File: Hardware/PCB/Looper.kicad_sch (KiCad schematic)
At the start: 63 parts, among them J1 Out right, J10 Audio from Daisy, connect to 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, J13 Audio to Daisy, connect to J13, J14 Audio from Daisy, connect to 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, J15 Audio input, connect to J18, J16 Audio output, connect to J17, J17 Audio output, connect to J16, J18 Audio input, connect to J15, J2 In left, J3 Trig Loop, J4 Out left, J5 In right, J6 Eurorack_Power, J9 Audio to Daisy, connect to J13, U1 TL074, U2 TL074

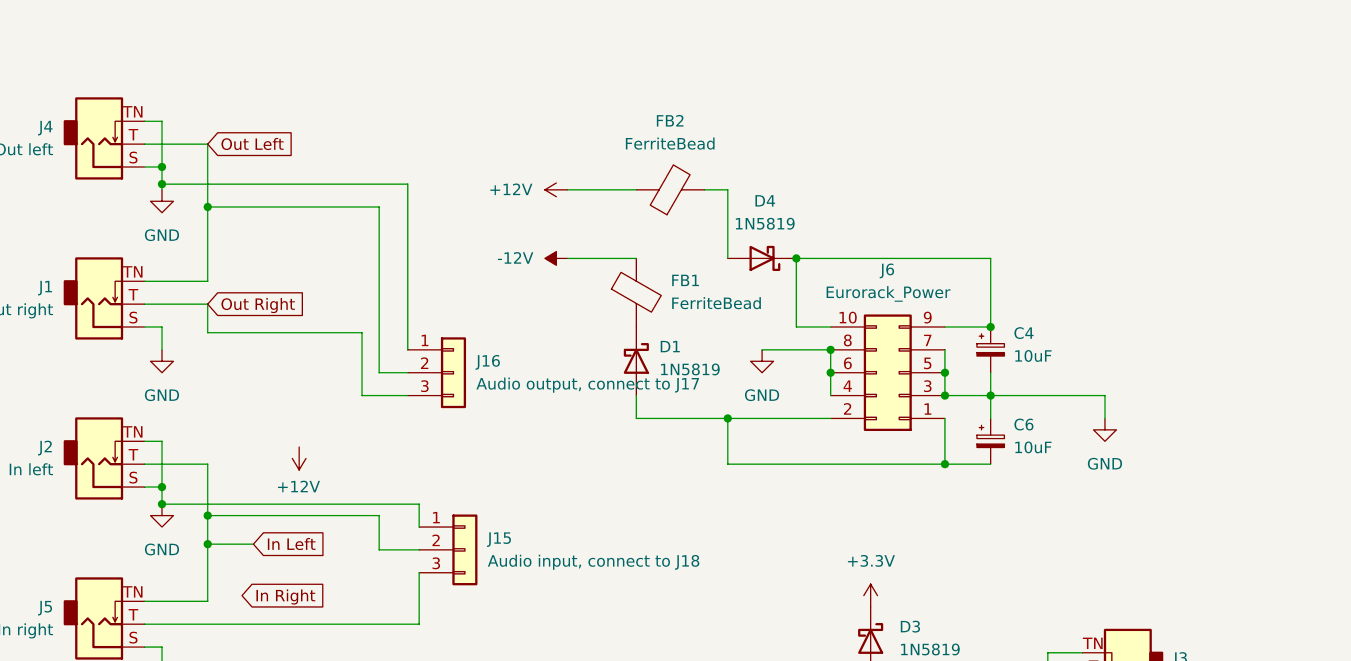
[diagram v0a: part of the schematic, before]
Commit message: Fixed power diode polarity
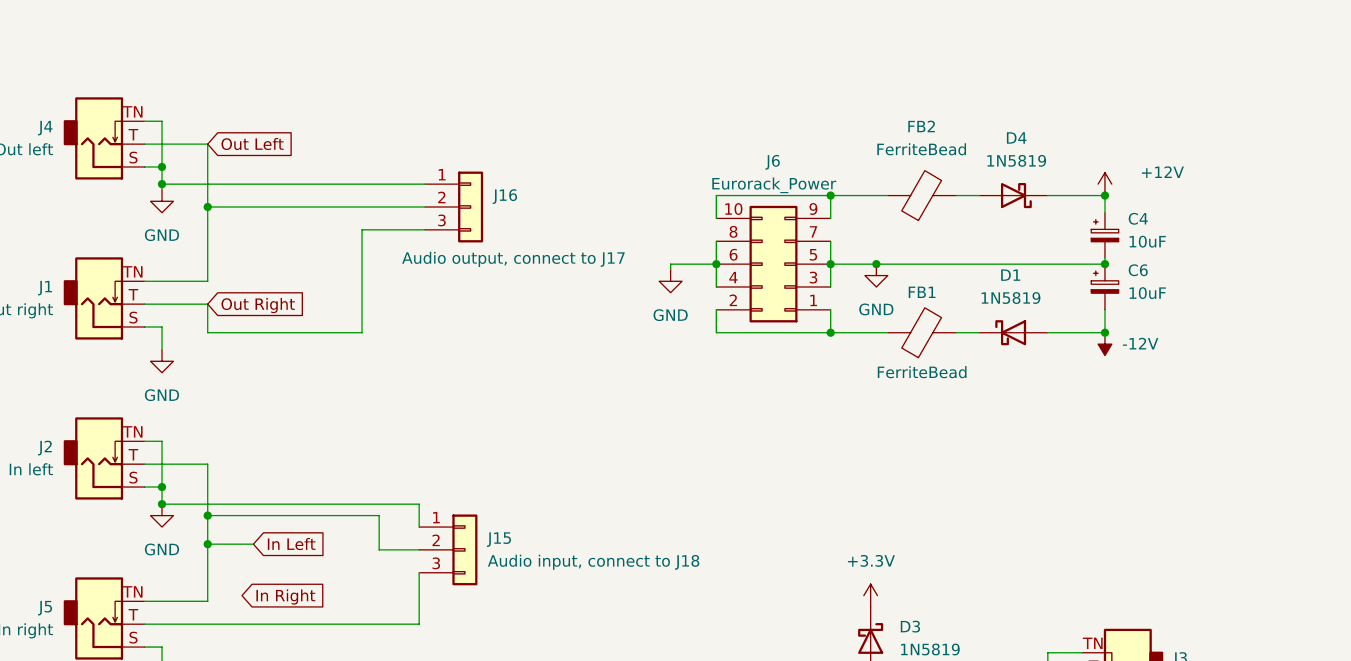
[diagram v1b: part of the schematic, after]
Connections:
- net +12V: now also C4.1, D4.1 (K); no longer FB2.1
- net -12V: now also C6.2, D1.2 (A); no longer FB1.1
- net at J6.10 (Pin_10), J6.9 (Pin_9): now also FB2.1; no longer C4.1, D4.1 (K)
- net at J6.1 (Pin_1), J6.2 (Pin_2): now also FB1.1; no longer C6.2, D1.2 (A)
- net at S1.1: now also A1.15 (USART1_RX)
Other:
- moved on the sheet: C4, C6, D1, D4, FB1, FB2, J16, J6

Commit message: new intracard connections
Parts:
- removed J10: Audio from Daisy, connect to J14, Connector_PinHeader_2.54mm:PinHeader_1x03_P2.54mm_Vertical, symbol Connector_Generic:Conn_01x03
- removed J13, J9: Audio to Daisy, connect to J13, Connector_PinHeader_2.54mm:PinHeader_1x03_P2.54mm_Vertical, symbol Connector_Generic:Conn_01x03
- removed J14: Audio from Daisy, connect to J10, Connector_PinHeader_2.54mm:PinHeader_1x03_P2.54mm_Vertical, symbol Connector_Generic:Conn_01x03
- removed J15: Audio input, connect to J18, Connector_PinHeader_2.54mm:PinHeader_1x03_P2.54mm_Vertical, symbol Connector_Generic:Conn_01x03
- removed J16: Audio output, connect to J17, Connector_PinHeader_2.54mm:PinHeader_1x03_P2.54mm_Vertical, symbol Connector_Generic:Conn_01x03
- removed J17: Audio output, connect to J16, Connector_PinHeader_2.54mm:PinHeader_1x03_P2.54mm_Vertical, symbol Connector_Generic:Conn_01x03
- removed J18: Audio input, connect to J15, Connector_PinHeader_2.54mm:PinHeader_1x03_P2.54mm_Vertical, symbol Connector_Generic:Conn_01x03
- added J11, J12, J7, J8: Conn_01x05, Connector_PinHeader_2.54mm:PinHeader_1x05_P2.54mm_Vertical, symbol Connector_Generic:Conn_01x05
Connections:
- net Out_R is gone; now on net DAISY_AUDIO_OUT_R: A1.19 (AUDIO_OUT_R)
- net +12V: now also J11.5 (Pin_5), J7.5 (Pin_5)
- net GND: now also J12.1 (Pin_1), J8.1 (Pin_1)
- net In Left: now also R16.1, J11.1 (Pin_1), J7.1 (Pin_1)
- net In Right: now also J5.T, R22.1, J12.2 (Pin_2), J8.2 (Pin_2)
- net Out Left: now also R5.1, U1.3 (+), J11.4 (Pin_4), J7.4 (Pin_4)
- net Out Right: now also R9.1, U1.10 (+), J12.4 (Pin_4), J8.4 (Pin_4)
- net at S1.1: now also A1.15 (USART1_RX)
- net DAISY_AUDIO_OUT_R: now reaches R21.2
- net DAISY_AUDIO_OUT_R: now also J12.3 (Pin_3), J8.3 (Pin_3)
- net DAISY_AUDIO_IN_L: now reaches A1.16 (AUDIO_IN_L)
- net DAISY_AUDIO_IN_L: now also R8.2, J11.3 (Pin_3), J7.3 (Pin_3)
- net DAISY_AUDIO_IN_R: now reaches A1.17 (AUDIO_IN_R)
- net DAISY_AUDIO_IN_R: now also R12.2, J12.5 (Pin_5), J8.5 (Pin_5)
- net DAISY_AUDIO_OUT_L: now reaches A1.18 (AUDIO_OUT_L)
- net DAISY_AUDIO_OUT_L: now also R14.2, J11.2 (Pin_2), J7.2 (Pin_2)
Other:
- moved on the sheet: J1, J2, J4, J5

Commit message: more labels
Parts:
- added J9: Conn_01x20_MountingPin, Connector_PinHeader_2.54mm:PinHeader_1x20_P2.54mm_Vertical, symbol Connector_Generic_MountingPin:Conn_01x20_MountingPin
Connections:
- net DAISY_AUDIO_IN_L: now also J9.16 (Pin_16)
- net DAISY_AUDIO_IN_R: now also J9.17 (Pin_17)
- net DAISY_AUDIO_OUT_L: now also J9.18 (Pin_18)
- net DAISY_AUDIO_OUT_R: now also J9.19 (Pin_19)
- net GND: now also J9.20 (Pin_20)
- net at R4.1: now also SW4.4; no longer A1.3 (SDMMC1_D2)
- net at R4.2: now also A1.3 (SDMMC1_D2), J9.3 (Pin_3); no longer SW4.4
- net at S1.1: now also A1.15 (USART1_RX), J9.15 (Pin_15)
- net at A1.2 (SDMMC1_D3), SW4.1: now also J9.2 (Pin_2)
- net at A1.4 (SDMMC1_D1), SW4.3: now also J9.4 (Pin_4)
- net at A1.14 (USART1_TX), S2.1: now also J9.14 (Pin_14)
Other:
- moved on the sheet: C1, C11, C12, C4, C5, C6, D1, D4, FB1, FB2, J1, J6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

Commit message: Endret hele leveller
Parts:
- removed D2, D3: 1N5819, Diode_SMD:D_SOD-123, symbol Device:D_Schottky
- added C13: 560pF, Capacitor_SMD:C_0603_1608Metric, symbol Device:C_Small
- added C14: 47pF, Capacitor_SMD:C_0603_1608Metric, symbol Device:C_Small
- added Q1: MMBT3904, Package_TO_SOT_SMD:SOT-23, symbol Transistor_BJT:MMBT3904
- added R23, R24, R25: 100K, Resistor_SMD:R_0603_1608Metric, symbol Device:R
- added R26: 10K, Resistor_SMD:R_0603_1608Metric, symbol Device:R
- added R27: 1K, Resistor_SMD:R_0603_1608Metric, symbol Device:R
- added R28: 1M, Resistor_SMD:R_0603_1608Metric, symbol Device:R
- C2: value 560pF -> 47pF; LCSC C458906 -> C1671
- R11: value 10K -> 100K; LCSC C25804 -> C25803
- R5: value 2M -> 10K; LCSC C22976 -> C25804
- R9: value 2M -> 100K; LCSC C22976 -> C25803
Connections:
- net +12V: now also J11.1 (Pin_1), J7.1 (Pin_1); no longer J11.5 (Pin_5), J7.5 (Pin_5)
- net +3.3V: now also R26.1
- net DAISY_AUDIO_IN_L: now also J12.2 (Pin_2), J8.2 (Pin_2), R16.1; no longer J11.3 (Pin_3), J7.3 (Pin_3), R8.2
- net DAISY_AUDIO_IN_R: now also J12.3 (Pin_3), J8.3 (Pin_3), R22.1; no longer J12.5 (Pin_5), J8.5 (Pin_5), R12.2
- net DAISY_AUDIO_OUT_L: now also J12.4 (Pin_4), J8.4 (Pin_4), R7.1; no longer J11.2 (Pin_2), J7.2 (Pin_2), R14.2
- net DAISY_AUDIO_OUT_R: now also J12.5 (Pin_5), J8.5 (Pin_5), R5.2; no longer J12.3 (Pin_3), J8.3 (Pin_3), R21.2
- net GND: now also J1.TN, J5.TN, U1.10 (+), U1.3 (+), Q1.2 (E), R28.2; no longer R5.2, R9.2
- net In Left: now also J11.2 (Pin_2), J7.2 (Pin_2), R17.2; no longer J11.1 (Pin_1), J5.TN, J7.1 (Pin_1), R16.1
- net In Right: now also J11.3 (Pin_3), J7.3 (Pin_3), R18.2; no longer J12.2 (Pin_2), J8.2 (Pin_2), R22.1
- net Out Left: now also R8.1; no longer J1.TN, R5.1, U1.3 (+)
- net Out Right: now also J11.5 (Pin_5), J7.5 (Pin_5), R12.2; no longer J12.4 (Pin_4), J8.4 (Pin_4), R9.1, U1.10 (+)
- net at SW4.4: now also R4.2; no longer R4.1
- net SWITCH_4_RED: now reaches A1.3 (SDMMC1_D2), J9.3 (Pin_3)
- net SWITCH_4_RED: now also R4.1; no longer R4.2
- net at J3.T: now also R11.2; no longer A1.22 (ADC_INP10)
- net at C10.2, R19.2: now also R18.1, U2.2 (-); no longer R21.1, U2.13 (-)
- net at C10.1, R19.1, R20.2: now also U2.1; no longer U2.14
- net CLEAR_GPIO: now reaches S1.1
- net CLEAR_GPIO: now also A1.15 (USART1_RX), J9.15 (Pin_15)
- net SWITCH_4_GPIO: now reaches A1.2 (SDMMC1_D3), J9.2 (Pin_2), SW4.1
- net SWITCH_4_GREEN: now reaches A1.4 (SDMMC1_D1), J9.4 (Pin_4), SW4.3
- net at R6.2, U1.6 (-): now also C14.1, R24.1; no longer C2.1, R7.1
- net RECORD_GPIO: now reaches A1.23 (ADC_INP15)
- net RECORD_GPIO: now also S2.1
- net SWITCH_1_GREEN: now reaches A1.27 (ADC_INP11), SW1.3
- net SWITCH_1_RED: now reaches A1.28 (ADC1_INP4), R3.2
- net SWITCH_1_GPIO: now reaches A1.29 (DAC1_OUT2), SW1.1
- net SWITCH_2_RED: now reaches A1.30 (DAC1_OUT1), SW2.4
- net SWITCH_2_GPIO: now reaches A1.31 (SAI2_MCLK_B), SW2.2
- net at R2.2: now also SW2.3; no longer A1.32 (SAI2_SD_B)
- net SWITCH_3_GREEN: now reaches A1.33 (SAI2_SD_A), SW3.3
- net SWITCH_3_GPIO: now reaches A1.34 (SAI2_FS_B), SW3.1
- net at R1.1: now also SW3.4; no longer A1.35 (SAI2_SCK_B)
- net at C7.1, R13.1: now also R17.1, U2.6 (-); no longer R14.1, U2.2 (-)
- net SWITCH_2_GREEN: now reaches R2.1
- net SWITCH_2_GREEN: now also A1.32 (SAI2_SD_B); no longer SW2.3
- net at C7.2, R13.2, R15.2: now also U2.7; no longer U2.1
- net SWITCH_3_RED: now reaches R1.2
- net SWITCH_3_RED: now also A1.35 (SAI2_SCK_B); no longer SW3.4
- new net: C14.2, R24.2, R8.2, U1.7
- new net: C3.1, R20.1, R21.2, U2.13 (-)
- new net: C3.2, R21.1, R22.2, U2.14
- new net: C9.1, R10.1, R9.2, U1.14
- new net: C9.2, R5.1, R9.1, U1.13 (-)
- new net: C13.2, R14.1, R16.2, U2.8
- new net: C13.1, R14.2, R15.1, U2.9 (-)
- new net: C8.1, R23.1, R7.2, U1.9 (-)
- new net: C2.1, R12.1, R25.2, U1.1
- new net: C2.2, R10.2, R25.1, U1.2 (-)
- new net: C8.2, R23.2, R6.1, U1.8
- new net: Q1.3 (C), R26.2, R27.2
- new net: Q1.1 (B), R11.1, R28.1
- new net TRIG_GPIO: A1.22 (ADC_INP10), R27.1
- now unconnected: A1.14 (USART1_TX), J9.14 (Pin_14)
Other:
- moved on the sheet: C10, C3, C4, C6, C7, C9, D1, D4, FB1, FB2, J1, J11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

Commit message: HW 1.0c
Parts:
- removed J9: Conn_01x20_MountingPin, Connector_PinHeader_2.54mm:PinHeader_1x20_P2.54mm_Vertical, symbol Connector_Generic_MountingPin:Conn_01x20_MountingPin
- removed R28: 1M, Resistor_SMD:R_0603_1608Metric, symbol Device:R
- added R29: 100K, Resistor_SMD:R_0603_1608Metric, symbol Device:R
- A1: now left out of the parts list
- Q1: LCSC (none) -> C20526
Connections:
- net GND: now also R29.1
- net RECORD_GPIO: now also A1.22 (ADC_INP10); no longer A1.23 (ADC_INP15)
- net SWITCH_1_GPIO: now also A1.26 (ADC_INP3); no longer A1.29 (DAC1_OUT2)
- net SWITCH_1_GREEN: now also A1.24 (ADC_INP5); no longer A1.27 (ADC_INP11)
- net SWITCH_1_RED: now also A1.25 (ADC_INP7); no longer A1.28 (ADC1_INP4)
- net SWITCH_2_GPIO: now also A1.27 (ADC_INP11); no longer A1.31 (SAI2_MCLK_B)
- net SWITCH_2_GREEN: now also A1.29 (DAC1_OUT2); no longer A1.32 (SAI2_SD_B)
- net SWITCH_2_RED: now also A1.28 (ADC1_INP4); no longer A1.30 (DAC1_OUT1)
- net TRIG_GPIO: now also A1.23 (ADC_INP15); no longer A1.22 (ADC_INP10)
- net at Q1.1 (B), R11.1: now also R29.2
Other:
- moved on the sheet: A1, C1, C10, C11, C12, C13, C14, C2, C3, C4, C5, C6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

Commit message: Version 1.0d hardware
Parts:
- removed J11, J7: Conn_01x05, Connector_PinHeader_2.54mm:PinHeader_1x05_P2.54mm_Vertical, symbol Connector_Generic:Conn_01x05
- added J10: Conn_01x06_Socket, Connector_PinHeader_2.54mm:PinHeader_1x06_P2.54mm_Vertical, symbol Connector:Conn_01x06_Socket
- added J9: Conn_01x06_Pin, Connector_PinHeader_2.54mm:PinHeader_1x06_P2.54mm_Vertical, symbol Connector:Conn_01x06_Pin
- R1, R2, R3, R4: LCSC (none) -> C22796
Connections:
- net +12V: now also J10.2 (Pin_2), J9.2 (Pin_2)
- net GND: now also J10.1 (Pin_1), J9.1 (Pin_1); no longer A1.20 (AGND), C1.1, C11.2, C12.1, C5.2, J1.S, J1.TN, J12.1 (Pin_1), J2.S, J2.TN, J4.S, J4.TN, J5.S, J5.TN, J8.1 (Pin_1), U1.10 (+), U1.12 (+), U1.3 (+), U1.5 (+), U2.10 (+), U2.12 (+), U2.3 (+), U2.5 (+)
- net In Left: now also J10.6 (Pin_6), J9.6 (Pin_6)
- net In Right: now also J10.5 (Pin_5), J9.5 (Pin_5)
- net Out Left: now also J10.4 (Pin_4), J9.4 (Pin_4)
- net Out Right: now also J10.3 (Pin_3), J9.3 (Pin_3)
- net SWITCH_1_RED: now also A1.14 (USART1_TX); no longer A1.25 (ADC_INP7)
- new net AGND: A1.20 (AGND), C1.1, C11.2, C12.1, C5.2, J1.S, J1.TN, J12.1 (Pin_1), J2.S, J2.TN, J4.S, J4.TN, J5.S, J5.TN, J8.1 (Pin_1), U1.10 (+), U1.12 (+), U1.3 (+), U1.5 (+), U2.10 (+), U2.12 (+), U2.3 (+), U2.5 (+)
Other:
- moved on the sheet: A1
